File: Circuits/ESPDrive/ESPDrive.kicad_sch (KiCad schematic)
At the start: 51 parts, among them Q1 AOSS32334C, U1 AP63203WU, U2 AP63201WU, U3 LTV-827S

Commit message: ESPDrive: Final tweaks before manufacture
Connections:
- net C_en: now also MCU1.30 (D23); no longer MCU1.22 (TX2)
- net C_vdiv: now also MCU1.4 (D34); no longer MCU1.20 (D4)
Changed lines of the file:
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@@
 	)
 	(no_connect
-		(at 252.73 64.77)
+		(at 252.73 57.15)
 	)
 	(no_connect
@@
 	)
 	(no_connect
-		(at 252.73 82.55)
+		(at 222.25 64.77)
 	)
 	(no_connect
@@
 	(wire
 		(pts
-			(xy 222.25 64.77) (xy 218.44 64.77)
+			(xy 252.73 82.55) (xy 256.54 82.55)
 		)
 		(stroke
@@
 	(wire
 		(pts
-			(xy 252.73 57.15) (xy 257.81 57.15)
+			(xy 252.73 64.77) (xy 257.81 64.77)
 		)
 		(stroke
@@
 	(global_label "C_vdiv"
 		(shape input)
-		(at 218.44 64.77 180)
+		(at 256.54 82.55 0)
 		(fields_autoplaced yes)
 		(effects
@@
 				(size 1.1 1.1)
 			)
-			(justify right)
+			(justify left)
 		)
 		(property "Intersheetrefs" "${INTERSHEET_REFS}"
-			(at 210.7214 64.77 0)
+			(at 264.2586 82.55 0)
 			(hide yes)
 			(show_name no)
@@
 					(size 1.27 1.27)
 				)
-				(justify right)
+				(justify left)
 			)
 		)
@@
 	(global_label "C_en"
 		(shape output)
-		(at 257.81 57.15 0)
+		(at 257.81 64.77 0)
 		(fields_autoplaced yes)
 		(effects
@@
 		)
 		(property "Intersheetrefs" "${INTERSHEET_REFS}"
-			(at 264.2715 57.15 0)
+			(at 264.2715 64.77 0)
 			(hide yes)
 			(show_name no)

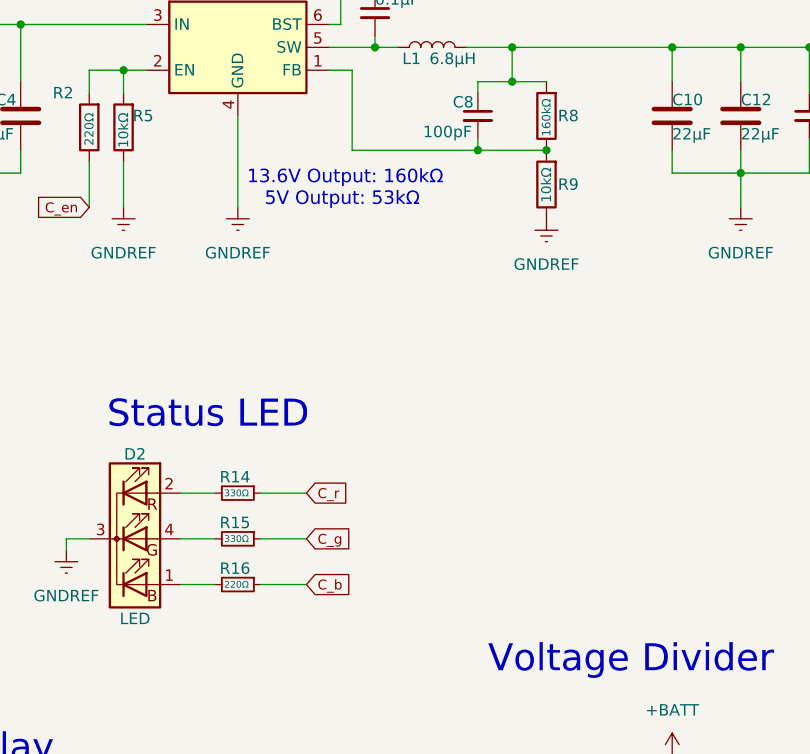
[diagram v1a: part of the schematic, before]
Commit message: ESPDrive: Slight tweaks, added ordered parts to BOM
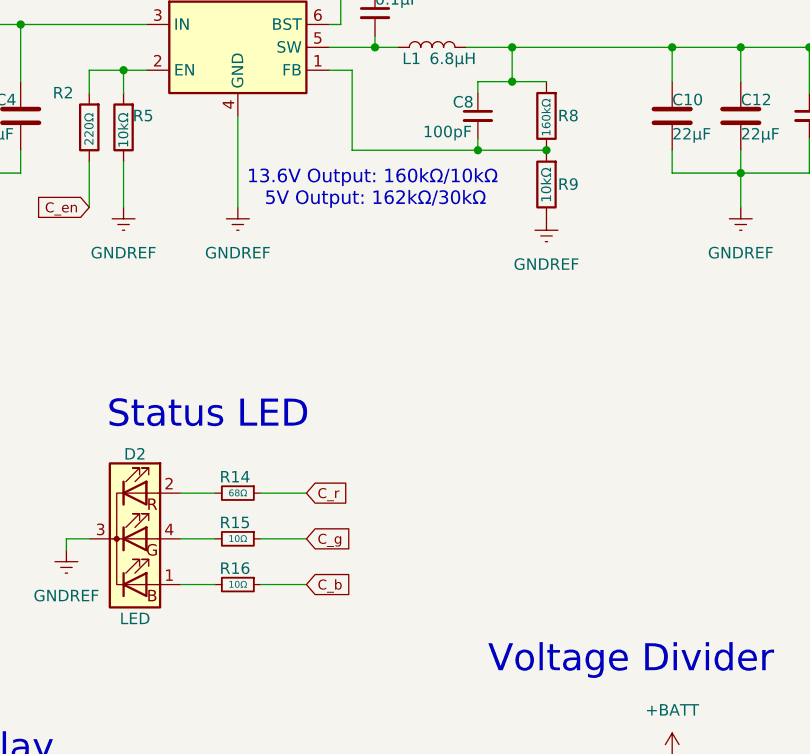
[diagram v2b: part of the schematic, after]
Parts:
- R14: value 330Ω -> 68Ω
- R15: value 330Ω -> 10Ω
- R16: value 220Ω -> 10Ω
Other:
- note added: "13.6V Output: 160kΩ/10kΩ 5V Output: 162kΩ/30kΩ"
- note removed: "13.6V Output: 160kΩ 5V Output: 53kΩ"
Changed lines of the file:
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@@
 		)
 	)
-	(text "13.6V Output: 160kΩ\n   5V Output: 53kΩ"
+	(text "13.6V Output: 160kΩ/10kΩ\n   5V Output: 162kΩ/30kΩ"
 		(exclude_from_sim no)
 		(at 108.966 91.948 0)
@@
 			)
 		)
-		(property "Value" "330Ω"
-			(at 106.426 130.81 90)
+		(property "Value" "10Ω"
+			(at 107.95 130.81 90)
 			(show_name no)
 			(do_not_autoplace no)
@@
 					(size 0.75 0.75)
 				)
-				(justify left)
 			)
 		)
@@
 			)
 		)
-		(property "Value" "220Ω"
-			(at 106.426 135.89 90)
+		(property "Value" "10Ω"
+			(at 107.95 135.89 90)
 			(show_name no)
 			(do_not_autoplace no)
@@
 					(size 0.75 0.75)
 				)
-				(justify left)
 			)
 		)
@@
 			)
 		)
-		(property "Value" "330Ω"
-			(at 106.426 125.73 90)
+		(property "Value" "68Ω"
+			(at 107.95 125.73 90)
 			(show_name no)
 			(do_not_autoplace no)
@@
 					(size 0.75 0.75)
 				)
-				(justify left)
 			)
 		)

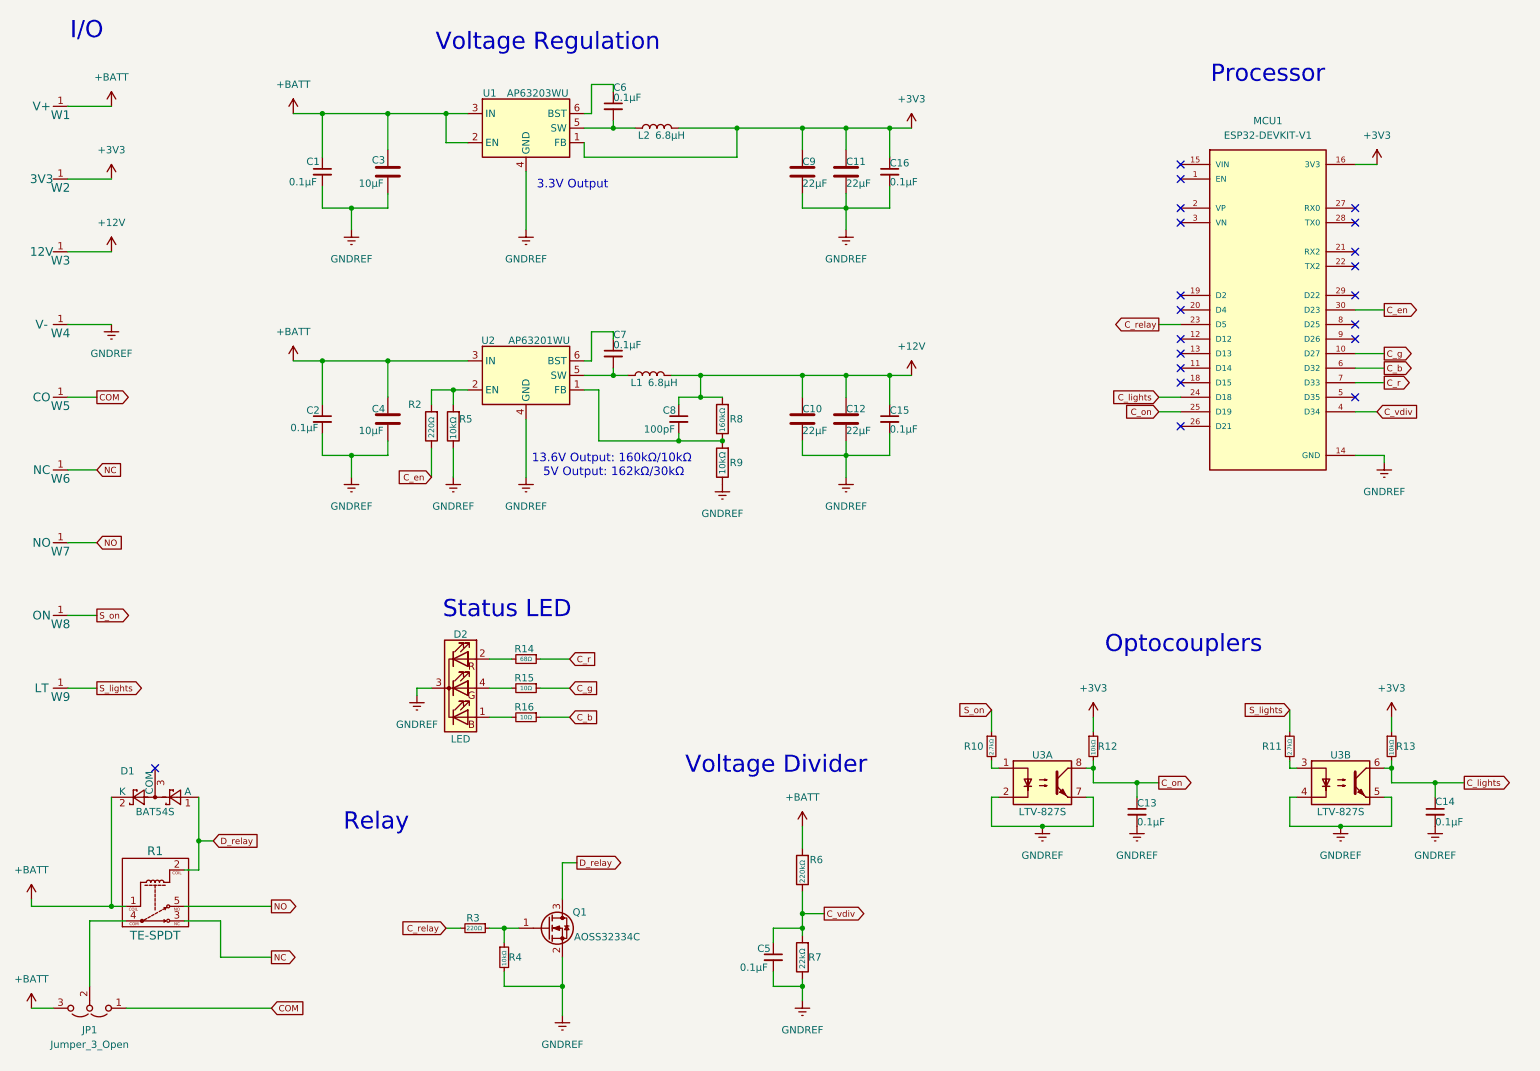
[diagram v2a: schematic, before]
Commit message: ESPDrive: Added p channel mosfet to voltage divider; versioned to v1.1
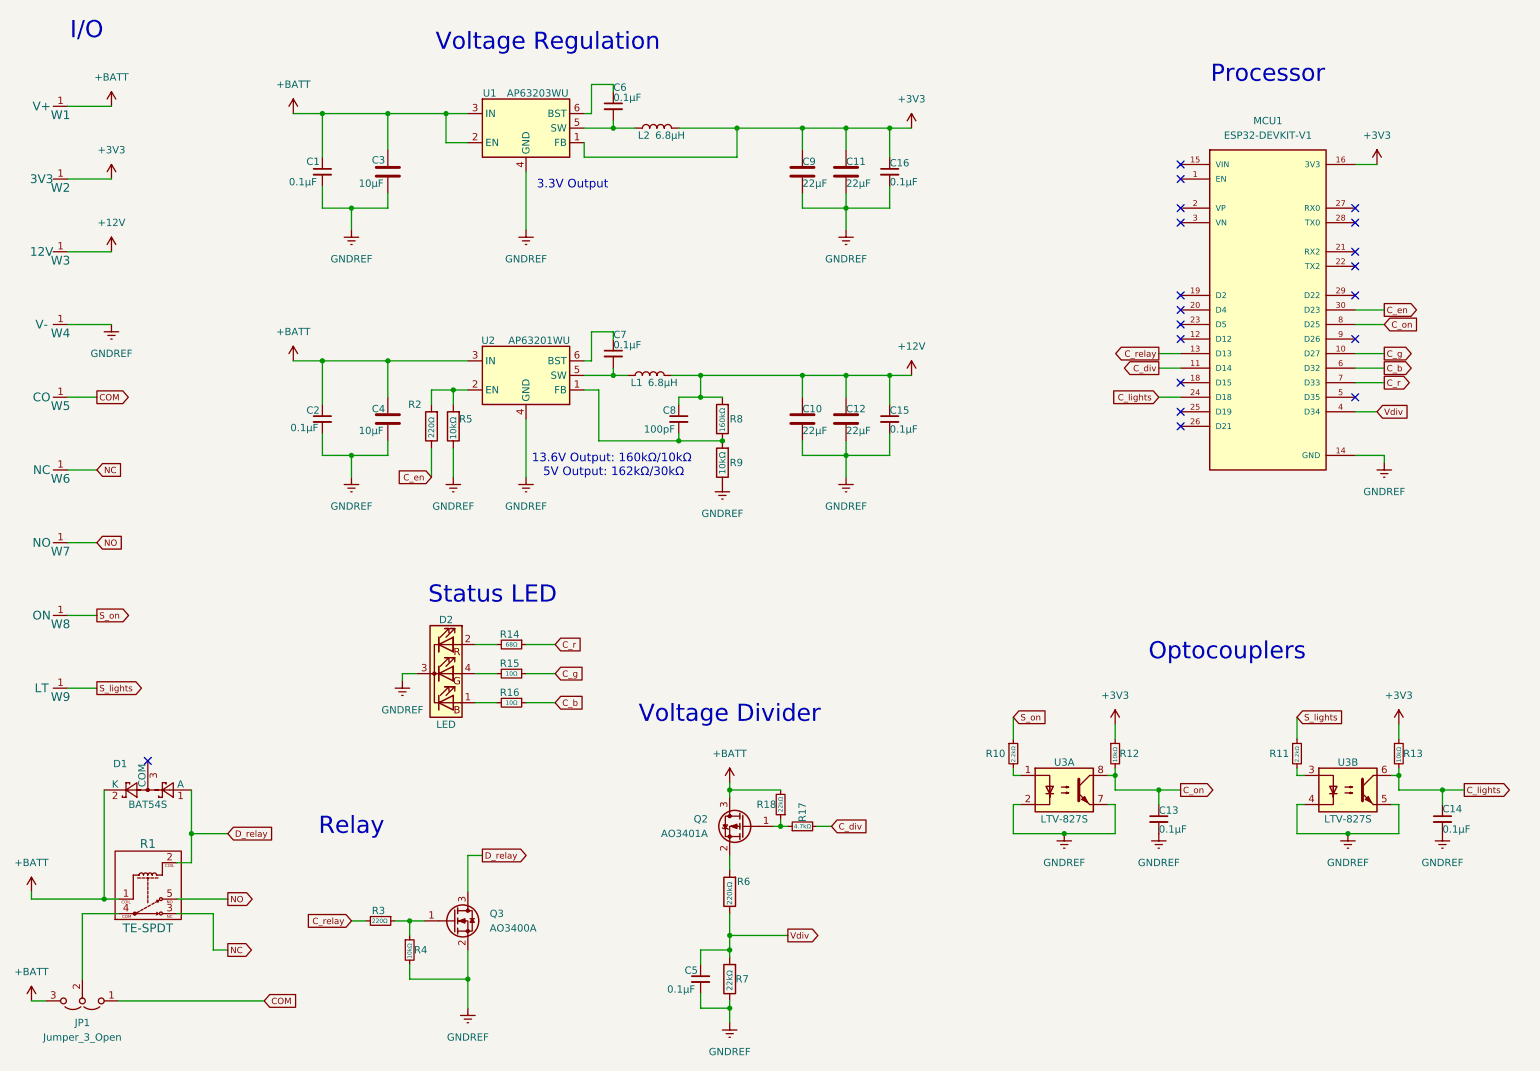
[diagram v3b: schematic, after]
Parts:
- removed Q1: AOSS32334C, Package_TO_SOT_SMD:SOT-23-3, symbol Transistor_FET:Q_NMOS_GSD
- added Q2: AO3401A, Package_TO_SOT_SMD:SOT-23, symbol Transistor_FET:AO3401A
- added Q3: AO3400A, Package_TO_SOT_SMD:SOT-23, symbol Transistor_FET:AO3400A
- added R17: 4.7kΩ, Resistor_SMD:R_0805_2012Metric_Pad1.20x1.40mm_HandSolder, symbol Device:R_Small
- added R18: 22kΩ, Resistor_SMD:R_0805_2012Metric_Pad1.20x1.40mm_HandSolder, symbol Device:R_Small
- L1, L2: footprint Inductor_SMD:L_TechFuse_SL0630 -> Inductor_SMD:L_Abracon_ASPI-0630LR
- R10, R11: value 2.7kΩ -> 2.2kΩ
- R6, R7, R8, R9: Precision (none) -> 0.5%
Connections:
- net +BATT: now also Q2.3 (D), R18.2; no longer R6.2
- net C_on: now also MCU1.8 (D25); no longer MCU1.25 (D19)
- net C_relay: now also MCU1.13 (D13); no longer MCU1.23 (D5)
- net D_relay: now also Q3.3 (D)
- net GND: now also Q3.2 (S)
- net at R3.1, R4.1: now also Q3.1 (G)
- net C_div: now reaches MCU1.11 (D14)
- net C_div: now also R17.2
- net C_vdiv renamed Vdiv
- new net: Q2.1 (G), R17.1, R18.1
- new net: Q2.2 (S), R6.2
- no-connect marks 20 -> 19
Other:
- moved on the sheet: C13, C14, C5, D1, D2, JP1, R1, R10, R11, R12, R13, R14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
